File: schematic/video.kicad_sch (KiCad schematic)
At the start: 9 parts, among them U10 MK4116P, U11 MK4116P, U12 MK4116P, U13 MK4116P, U14 MK4116P, U15 MK4116P, U16 MK4116P, U17 MK4116P, U9 TMS9928A

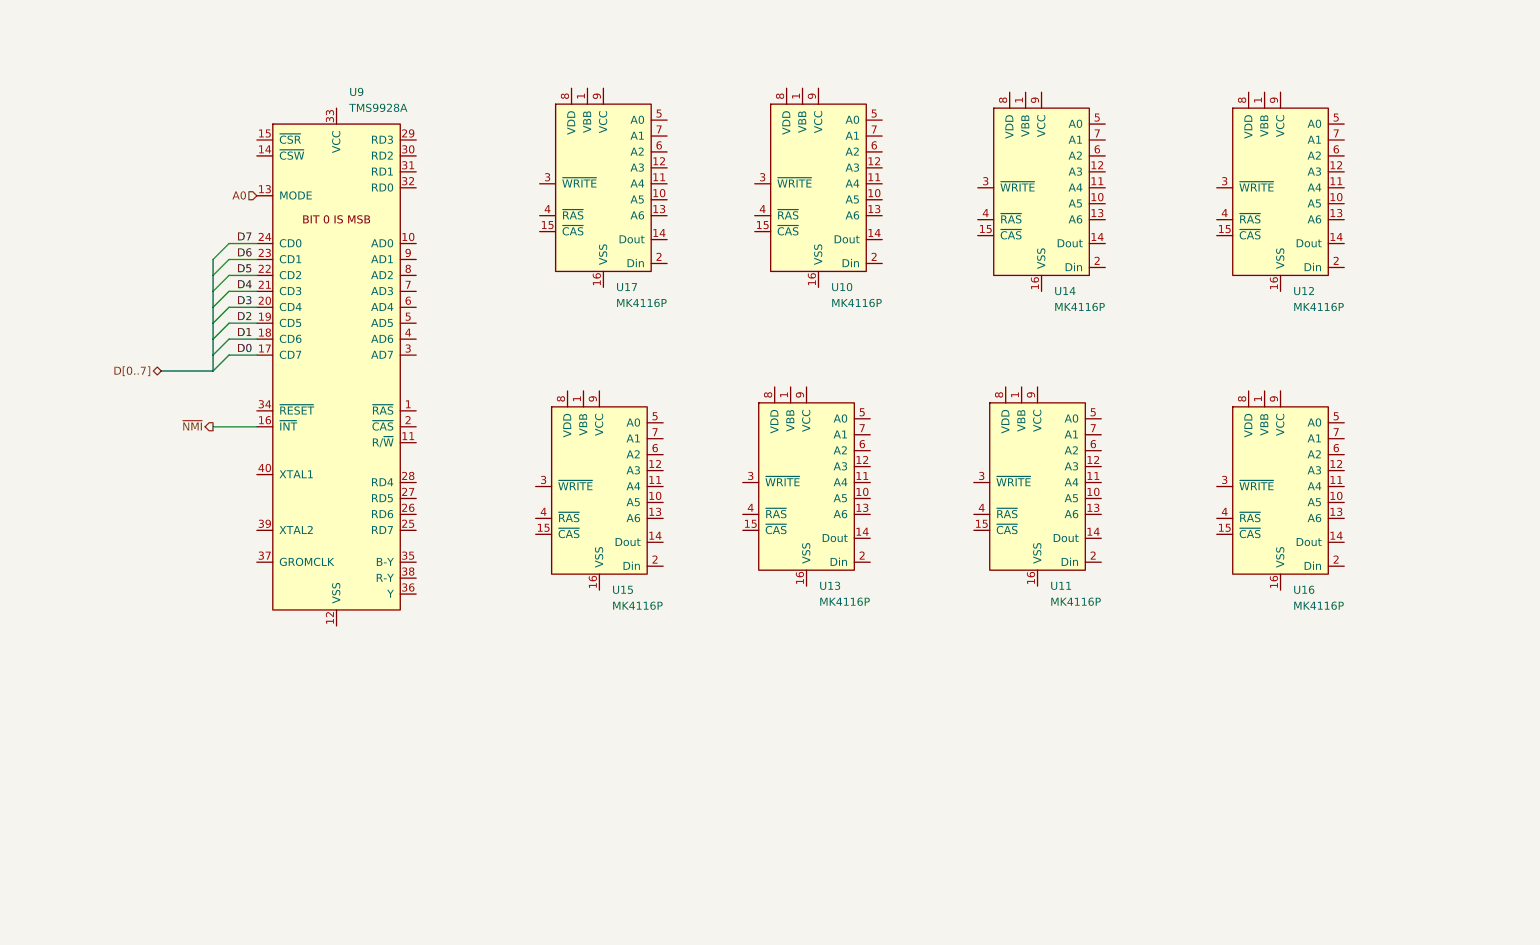
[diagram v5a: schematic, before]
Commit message: added rf modulation schematic, added dram to vdp. Fixed +5vc to +5v
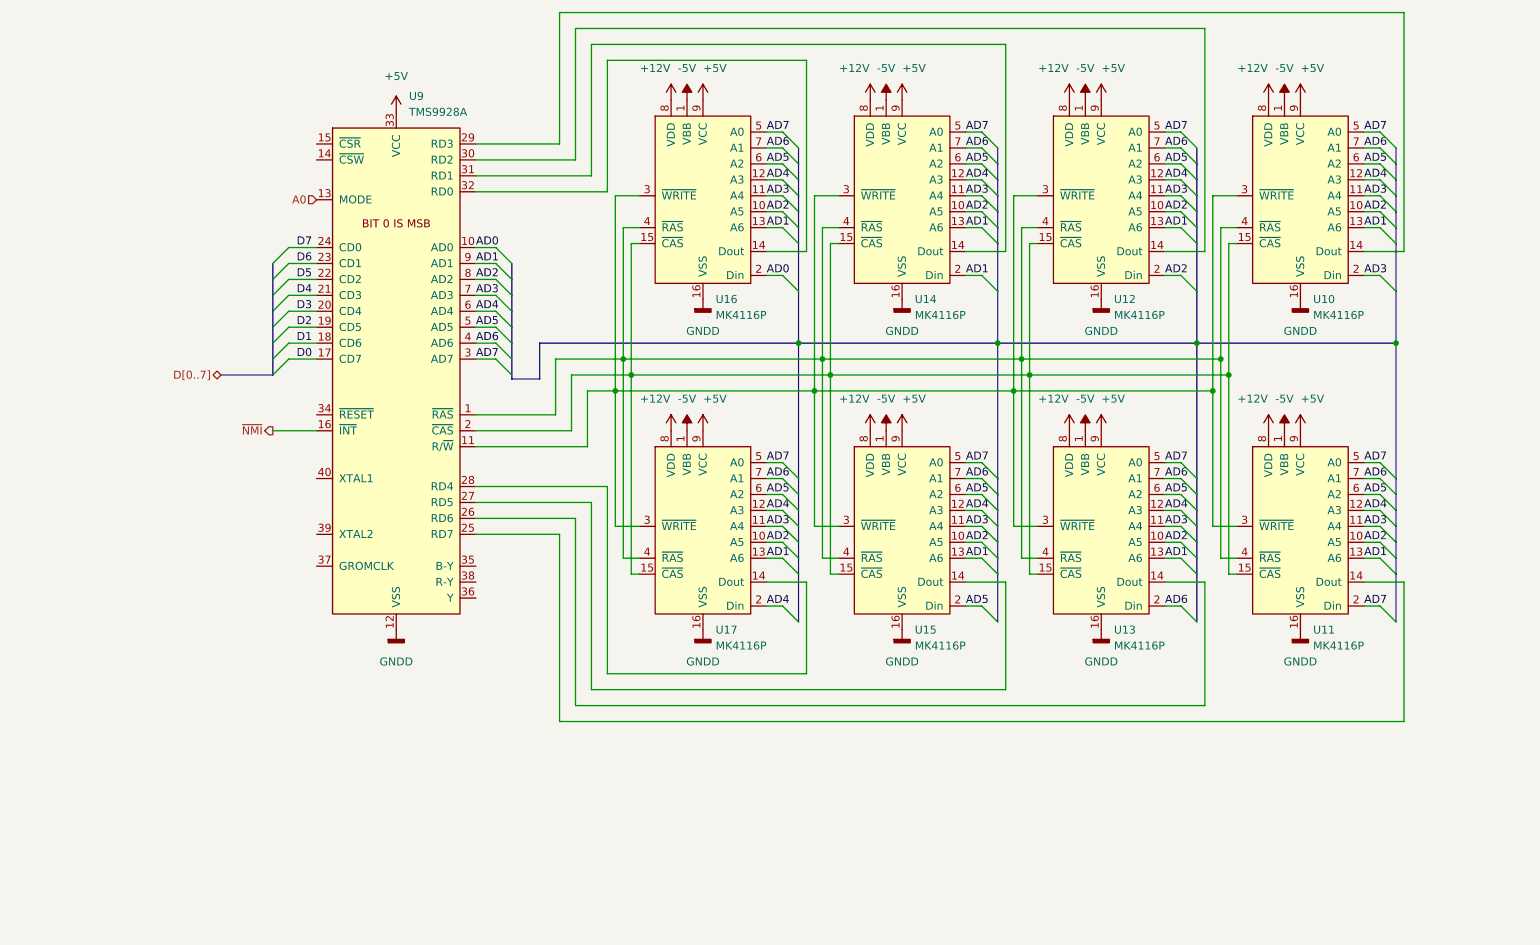
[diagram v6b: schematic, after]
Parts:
- renumbered U17 to U11, U15 to U13, U13 to U15, U11 to U17
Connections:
- net -5V: now reaches U17.1 (VBB)
- net -5V: now also U10.1 (VBB), U11.1 (VBB), U12.1 (VBB), U13.1 (VBB), U14.1 (VBB), U15.1 (VBB), U16.1 (VBB)
- net AD2: now reaches U17.10 (A5)
- net AD2: now also U10.10 (A5), U11.10 (A5), U12.10 (A5), U12.2 (Din), U13.10 (A5), U14.10 (A5), U15.10 (A5), U16.10 (A5), U9.8 (AD2)
- net AD3: now reaches U17.11 (A4)
- net AD3: now also U10.11 (A4), U10.2 (Din), U11.11 (A4), U12.11 (A4), U13.11 (A4), U14.11 (A4), U15.11 (A4), U16.11 (A4), U9.7 (AD3)
- net AD4: now reaches U17.12 (A3)
- net AD4: now also U10.12 (A3), U11.12 (A3), U12.12 (A3), U13.12 (A3), U14.12 (A3), U15.12 (A3), U16.12 (A3), U17.2 (Din), U9.6 (AD4)
- net AD1: now reaches U17.13 (A6)
- net AD1: now also U10.13 (A6), U11.13 (A6), U12.13 (A6), U13.13 (A6), U14.13 (A6), U14.2 (Din), U15.13 (A6), U16.13 (A6), U9.9 (AD1)
- net at U17.14 (Dout): now also U9.28 (RD4)
- net at U17.15 (~{CAS}): now also U10.15 (~{CAS}), U11.15 (~{CAS}), U12.15 (~{CAS}), U13.15 (~{CAS}), U14.15 (~{CAS}), U15.15 (~{CAS}), U16.15 (~{CAS}), U9.2 (~{CAS})
- net GNDD: now reaches U17.16 (VSS)
- net GNDD: now also U10.16 (VSS), U11.16 (VSS), U12.16 (VSS), U13.16 (VSS), U14.16 (VSS), U15.16 (VSS), U16.16 (VSS), U9.12 (VSS)
- net at U17.3 (~{WRITE}): now also U10.3 (~{WRITE}), U11.3 (~{WRITE}), U12.3 (~{WRITE}), U13.3 (~{WRITE}), U14.3 (~{WRITE}), U15.3 (~{WRITE}), U16.3 (~{WRITE}), U9.11 (R/~{W})
- net at U17.4 (~{RAS}): now also U10.4 (~{RAS}), U11.4 (~{RAS}), U12.4 (~{RAS}), U13.4 (~{RAS}), U14.4 (~{RAS}), U15.4 (~{RAS}), U16.4 (~{RAS}), U9.1 (~{RAS})
- net AD7: now reaches U17.5 (A0)
- net AD7: now also U10.5 (A0), U11.2 (Din), U11.5 (A0), U12.5 (A0), U13.5 (A0), U14.5 (A0), U15.5 (A0), U16.5 (A0), U9.3 (AD7)
- net AD5: now reaches U17.6 (A2)
- net AD5: now also U10.6 (A2), U11.6 (A2), U12.6 (A2), U13.6 (A2), U14.6 (A2), U15.2 (Din), U15.6 (A2), U16.6 (A2), U9.5 (AD5)
- net AD6: now reaches U17.7 (A1)
- net AD6: now also U10.7 (A1), U11.7 (A1), U12.7 (A1), U13.2 (Din), U13.7 (A1), U14.7 (A1), U15.7 (A1), U16.7 (A1), U9.4 (AD6)
- net +12V: now reaches U17.8 (VDD)
- net +12V: now also U10.8 (VDD), U11.8 (VDD), U12.8 (VDD), U13.8 (VDD), U14.8 (VDD), U15.8 (VDD), U16.8 (VDD)
- net +5V: now reaches U17.9 (VCC)
- net +5V: now also U10.9 (VCC), U11.9 (VCC), U12.9 (VCC), U13.9 (VCC), U14.9 (VCC), U15.9 (VCC), U16.9 (VCC), U9.33 (VCC)
- net at U16.14 (Dout): now also U9.32 (RD0)
- net AD0: now reaches U16.2 (Din)
- net AD0: now also U9.10 (AD0)
- net at U15.14 (Dout): now also U9.27 (RD5)
- net at U11.14 (Dout): now also U9.25 (RD7)
- net at U9.26 (RD6): now also U13.14 (Dout)
- net at U9.29 (RD3): now also U10.14 (Dout)
- net at U9.30 (RD2): now also U12.14 (Dout)
- net at U9.31 (RD1): now also U14.14 (Dout)
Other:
- moved on the sheet: U10, U11, U12, U13, U14, U15, U16, U17, U9

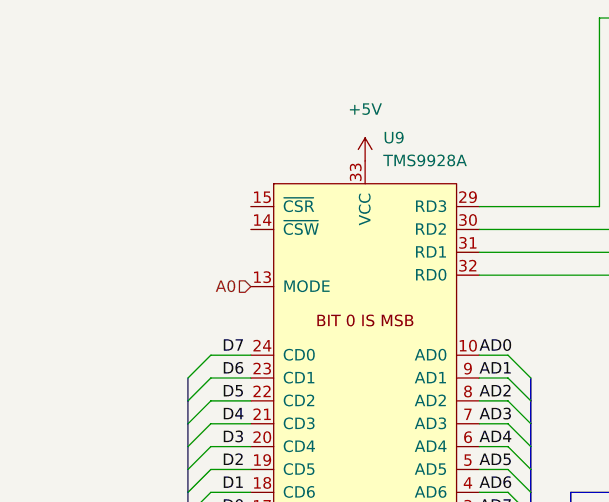
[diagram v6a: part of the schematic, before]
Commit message: added u6 decoder lines, renamed a few lines to make sense to there destination.
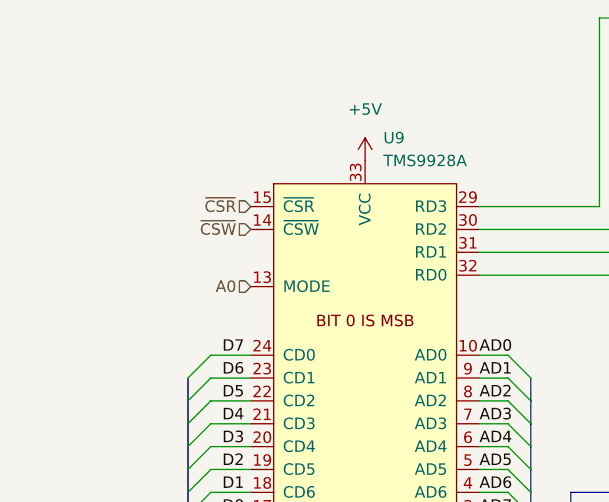
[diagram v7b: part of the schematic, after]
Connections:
- net ~{CSW}: now reaches U9.14 (~{CSW})
- net ~{CSR}: now reaches U9.15 (~{CSR})
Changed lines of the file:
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@@
     (effects (font (size 1.27 1.27)) (justify left bottom))
+  )
+  (hierarchical_label "~{CSW}" (shape input) (at 63.5 50.8 180)
+    (effects (font (size 1.27 1.27)) (justify right))
   )
   (hierarchical_label "D[0..7]" (shape bidirectional) (at 48.26 85.09 180)
     (effects (font (size 1.27 1.27)) (justify right))
   )
+  (hierarchical_label "~{CSR}" (shape input) (at 63.5 48.26 180)
+    (effects (font (size 1.27 1.27)) (justify right))
+  )
